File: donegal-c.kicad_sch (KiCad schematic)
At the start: 166 parts, among them J2 ISP, SW1 SW_SPST, SW10 SW_SPST, SW11 SW_SPST, SW12 SW_SPST, SW13 SW_SPST, SW14 SW_SPST, SW15 SW_SPST, SW16 SW_SPST, SW17 SW_SPST, SW18 SW_SPST, SW19 SW_SPST, SW2 SW_SPST, SW20 SW_SPST, SW21 SW_SPST, SW22 SW_SPST, SW23 SW_SPST, SW24 SW_SPST, SW25 SW_SPST, SW26 SW_SPST, SW27 SW_SPST, SW28 SW_SPST, SW29 SW_SPST, SW3 SW_SPST, SW30 SW_SPST, SW31 SW_SPST, SW32 SW_SPST, SW33 SW_SPST, SW34 SW_SPST, SW35 SW_SPST, SW36 SW_SPST, SW37 SW_SPST, SW38 SW_SPST, SW39 SW_SPST, SW4 SW_SPST, SW40 SW_SPST, SW41 SW_SPST, SW42 SW_SPST, SW43 SW_SPST, SW44 SW_SPST, SW45 SW_SPST, SW46 SW_SPST, SW47 SW_SPST, SW48 SW_SPST, SW49 SW_SPST, SW5 SW_SPST, SW50 SW_SPST, SW51 SW_SPST, SW52 SW_SPST, SW53 SW_SPST, SW54 SW_SPST, SW55 SW_SPST, SW56 SW_SPST, SW57 SW_SPST, SW58 SW_SPST, SW59 SW_SPST, SW6 SW_SPST, SW60 SW_SPST, SW61 SW_SPST, SW62 SW_SPST, SW63 SW_SPST, SW64 SW_SPST, SW65 SW_SPST, SW66 SW_SPST, SW67 SW_SPST, SW68 RESET, SW69 BOOT, SW7 SW_SPST, SW70 SW_SPST, SW71 SW_SPST, SW72 SW_SPST, SW8 SW_SPST, SW9 SW_SPST, U1 ATmega328-PU, Y1 16MHZ

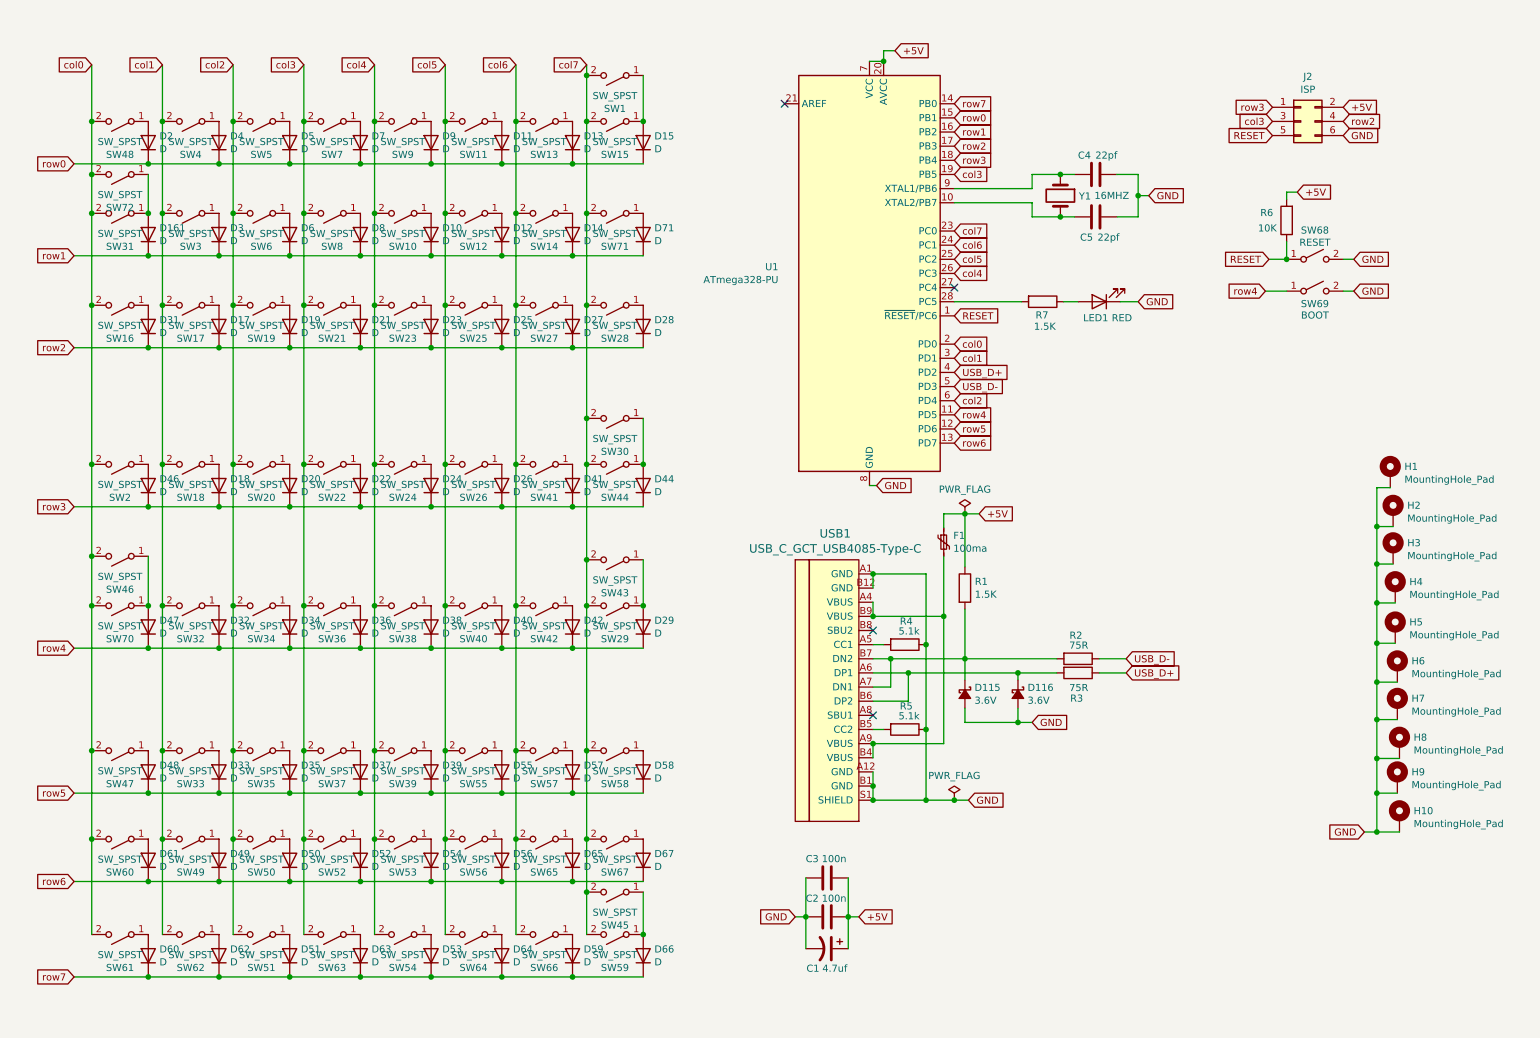
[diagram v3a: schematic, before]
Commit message: Update to v1.2
* Add Tsangan bottom row support
* Switch to MX_Alps_Hybrid MX_Only switch footprints
* Re-add the indicator LED to schematic
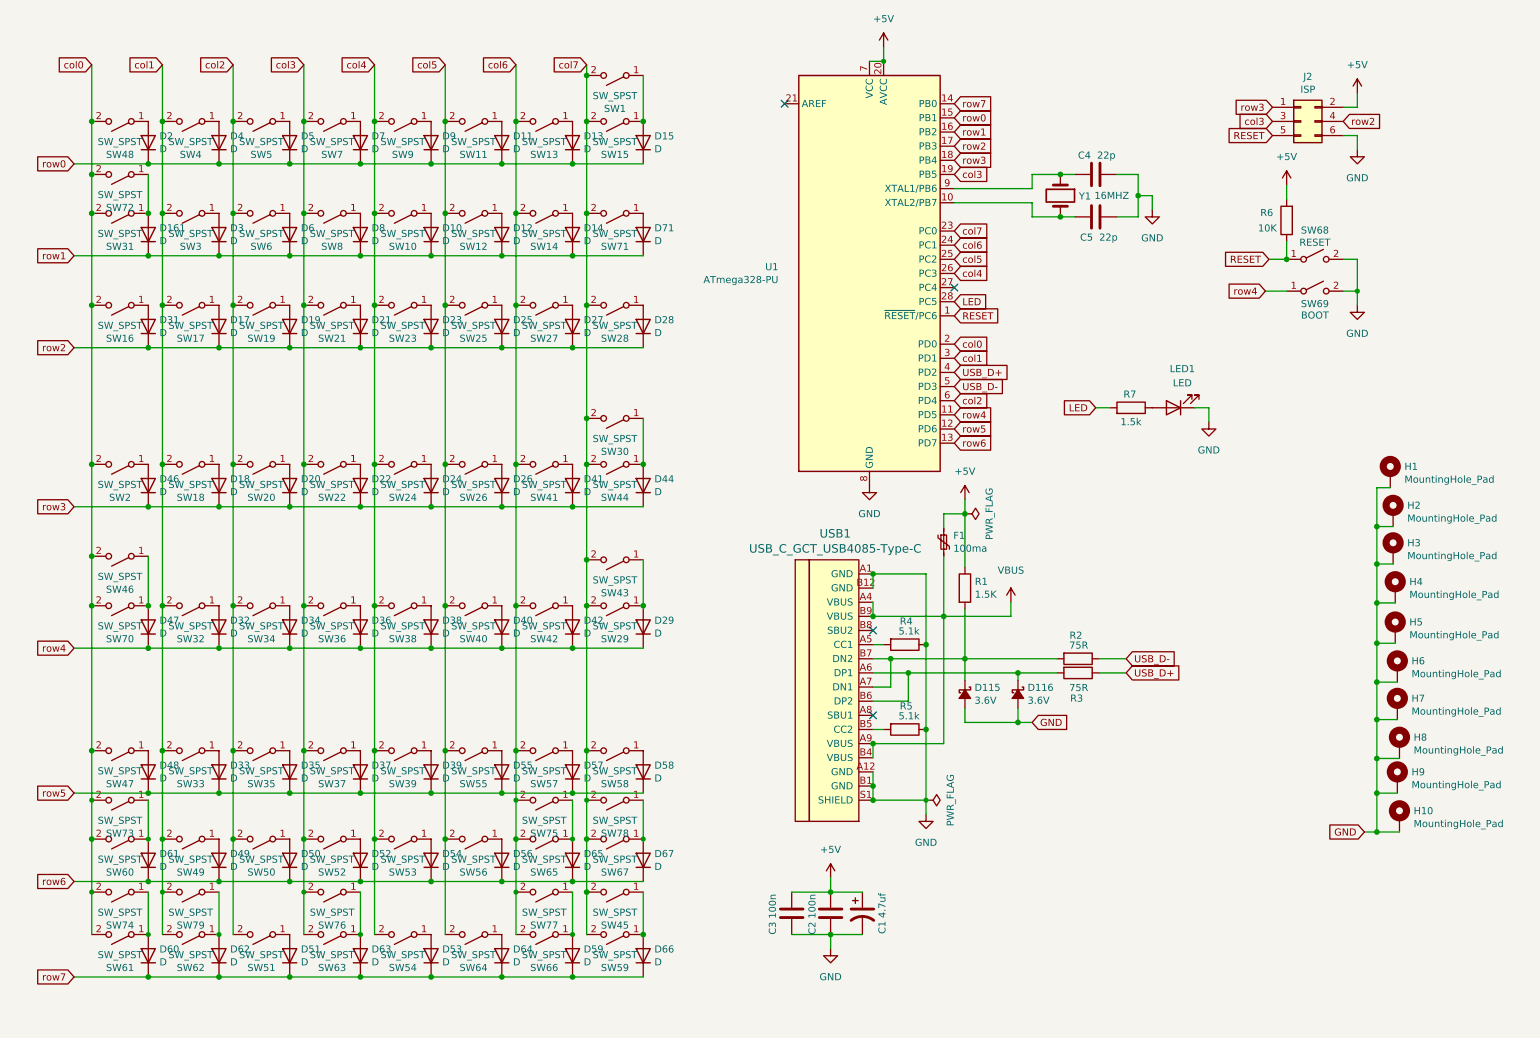
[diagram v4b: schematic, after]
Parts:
- added SW73, SW75, SW78, SW79: SW_SPST, MX_Only:MXOnly-1.5U-NoLED, symbol Switch:SW_SPST
- added SW74, SW77: SW_SPST, MX_Only:MXOnly-1U-NoLED, symbol Switch:SW_SPST
- added SW76: SW_SPST, MX_Only:MXOnly-7U-ReversedStabilizers-NoLED, symbol Switch:SW_SPST
- C4, C5: value 22pf -> 22p
- LED1: value RED -> LED
- R7: value 1.5K -> 1.5k
- SW1: footprint alpsmx:MX-2U-NoLED -> MX_Only:MXOnly-2U-NoLED
- SW10, SW11, SW12, SW13, SW14, SW15, SW17, SW18, SW19, SW2, SW20, SW21, SW22, SW23, SW24, SW25, SW26, SW27, SW28, SW29, SW3, SW32, SW33, SW34, SW35, SW36, SW37, SW38, SW39, SW4, SW40, SW41, SW42, SW47, SW48, SW49, SW5, SW50, SW51, SW52, SW53, SW54, SW55, SW56, SW57, SW58, SW6, SW7, SW71, SW8, SW9: footprint alpsmx:MX-1U-NoLED -> MX_Only:MXOnly-1U-NoLED
- SW16, SW43: footprint alpsmx:MX-1.5U-NoLED -> MX_Only:MXOnly-1.5U-NoLED
- SW30: footprint random:MX-ISO-ReversedStabilizersedit -> MX_Only:MXOnly-ISO-ROTATED-ReversedStabilizers-NoLED
- SW31: footprint tartan:SW_Cherry_MX1A_1.75u_PCBNOSCREEN -> MX_Only:MXOnly-1.75U-NoLED
- SW44, SW46: footprint alpsmx:MX-2.25U-NoLED -> MX_Only:MXOnly-2.25U-NoLED
- SW45: footprint alpsmx:MX-2.75U-NoLED -> MX_Only:MXOnly-2.75U-NoLED
- SW59: footprint alpsmx:MX-1.75U-NoLED -> MX_Only:MXOnly-1U-NoLED
- SW60, SW67, SW70: footprint alpsmx:MX-1.25U-NoLED -> MX_Only:MXOnly-1.25U-NoLED
- SW61, SW62, SW64, SW65, SW66: footprint alpsmx:MX-1.25U-NoLED -> MX_Only:MXOnly-1.5U-NoLED
- SW63: footprint alpsmx:MX-6.25U-ReversedStabilizers-NoLED -> MX_Only:MXOnly-6.25U-ReversedStabilizers-NoLED
- SW72: footprint tartan:SW_Cherry_MX1A_1.25u_PCBNOSCREEN -> MX_Only:MXOnly-1.25U-NoLED
- USB1: footprint tartan:USB_C_GCT_USB4085 -> 42keebs:USB_C_GCT_USB4085-offset-pads
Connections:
- net col0: now also SW73.2 (B), SW74.2 (B)
- net col1: now also SW79.2 (B)
- net col3: now also SW76.2 (B)
- net col6: now also SW75.2 (B), SW77.2 (B)
- net col7: now also SW78.2 (B)
- net at D61.2 (A), SW60.1 (A): now also SW73.1 (A)
- net at D65.2 (A), SW65.1 (A): now also SW75.1 (A)
- net at D67.2 (A), SW67.1 (A): now also SW78.1 (A)
- net at D59.2 (A), SW66.1 (A): now also SW77.1 (A)
- net at D60.2 (A), SW61.1 (A): now also SW74.1 (A)
- net at D62.2 (A), SW62.1 (A): now also SW79.1 (A)
- net at D63.2 (A), SW63.1 (A): now also SW76.1 (A)
- net LED: now reaches R7.2, U1.28 (PC5)
- net VBUS: now reaches F1.2, USB1.A4 (VBUS), USB1.A9 (VBUS), USB1.B4 (VBUS), USB1.B9 (VBUS)
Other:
- moved on the sheet: C1, C2, C3

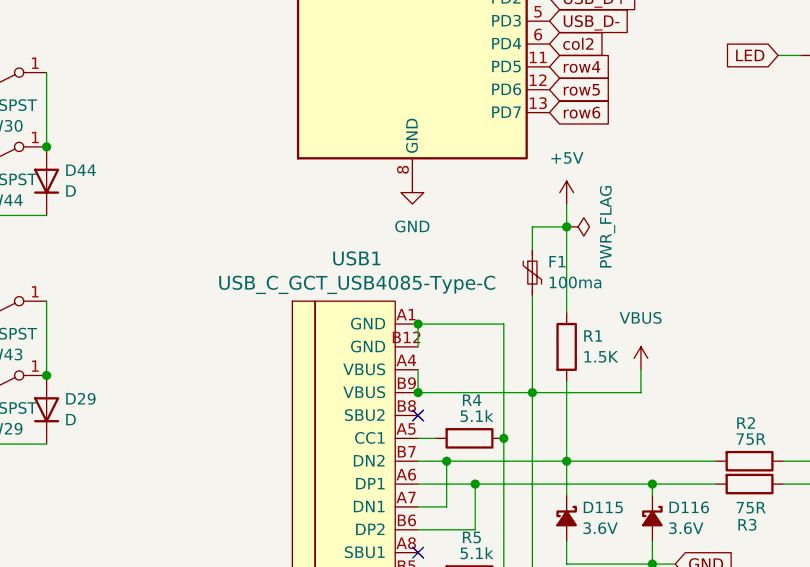
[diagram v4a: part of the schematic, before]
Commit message: Use USB-C socket symbol from the 42. Keebs library
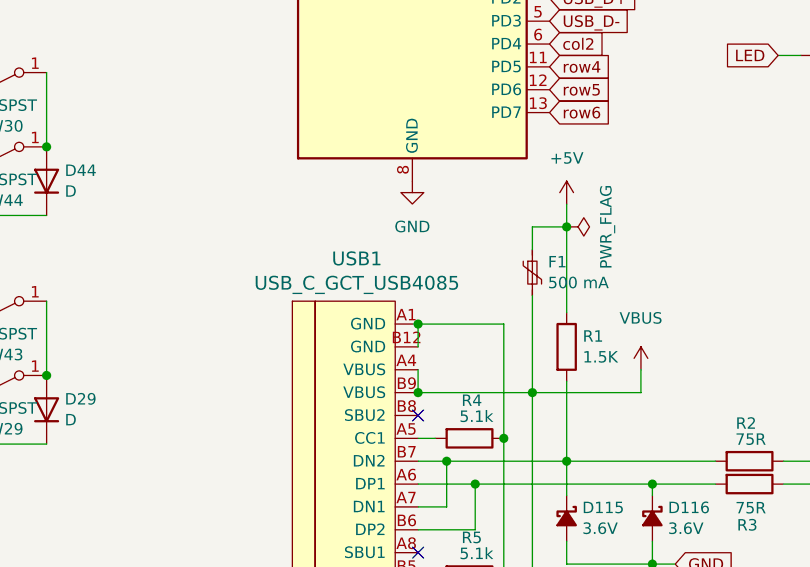
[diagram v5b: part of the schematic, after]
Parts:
- F1: value 100ma -> 500 mA
- USB1: value USB_C_GCT_USB4085-Type-C -> USB_C_GCT_USB4085; symbol donegal-c:USB_C_GCT_USB4085-Type-C -> 42keebs:USB_C_GCT_USB4085
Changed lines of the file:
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@@
       (effects (font (size 1.27 1.27)) (justify left))
     )
-    (property "Value" "100ma" (id 1) (at 179.5272 110.998 0)
+    (property "Value" "500 mA" (id 1) (at 179.5272 110.998 0)
       (effects (font (size 1.27 1.27)) (justify left))
     )
@@
     (pin "2")
   )
-  (symbol (lib_id "donegal-c:USB_C_GCT_USB4085-Type-C") (at 162.56 134.62 0) (unit 1)
+  (symbol (lib_id "42keebs:USB_C_GCT_USB4085") (at 162.56 134.62 0) (unit 1)
     (in_bom yes) (on_board yes)
     (property "Reference" "USB1" (id 0) (at 158.305 108.334 0)
       (effects (font (size 1.524 1.524)))
     )
-    (property "Value" "USB_C_GCT_USB4085-Type-C" (id 1) (at 158.3055 111.0411 0)
+    (property "Value" "USB_C_GCT_USB4085" (id 1) (at 158.3055 111.0411 0)
       (effects (font (size 1.524 1.524)))
     )
@@
     )
     (path "/00000000-0000-0000-0000-00005e210bf4"
-      (reference "F1") (unit 1) (value "100ma") (footprint "Capacitor_THT:C_Disc_D5.0mm_W2.5mm_P5.00mm")
+      (reference "F1") (unit 1) (value "500 mA") (footprint "Capacitor_THT:C_Disc_D5.0mm_W2.5mm_P5.00mm")
     )
     (path "/00000000-0000-0000-0000-00005df900c0"
@@
     )
     (path "/14cc5d03-4b82-4c1f-8c9a-4e49ee2a18b1"
-      (reference "USB1") (unit 1) (value "USB_C_GCT_USB4085-Type-C") (footprint "42keebs:USB_C_GCT_USB4085-offset-pads")
+      (reference "USB1") (unit 1) (value "USB_C_GCT_USB4085") (footprint "42keebs:USB_C_GCT_USB4085-offset-pads")
     )
     (path "/00000000-0000-0000-0000-00005e1e8d8f"

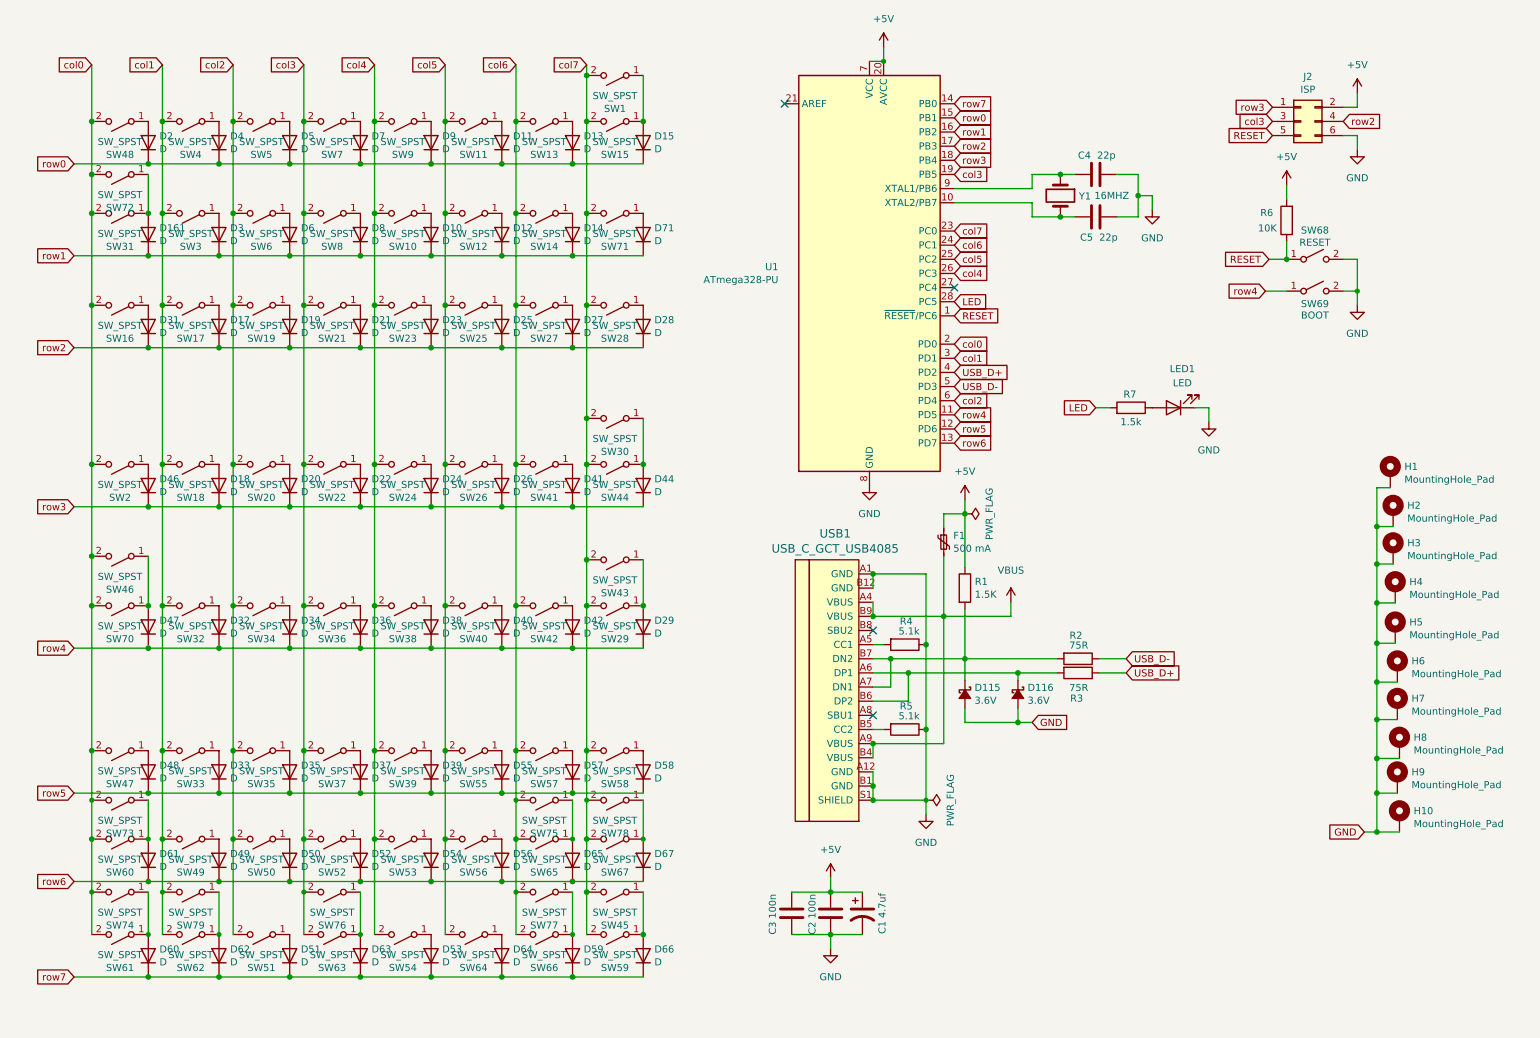
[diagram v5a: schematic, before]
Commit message: Fix incorrect bottom row sizes; add bottom row key labels
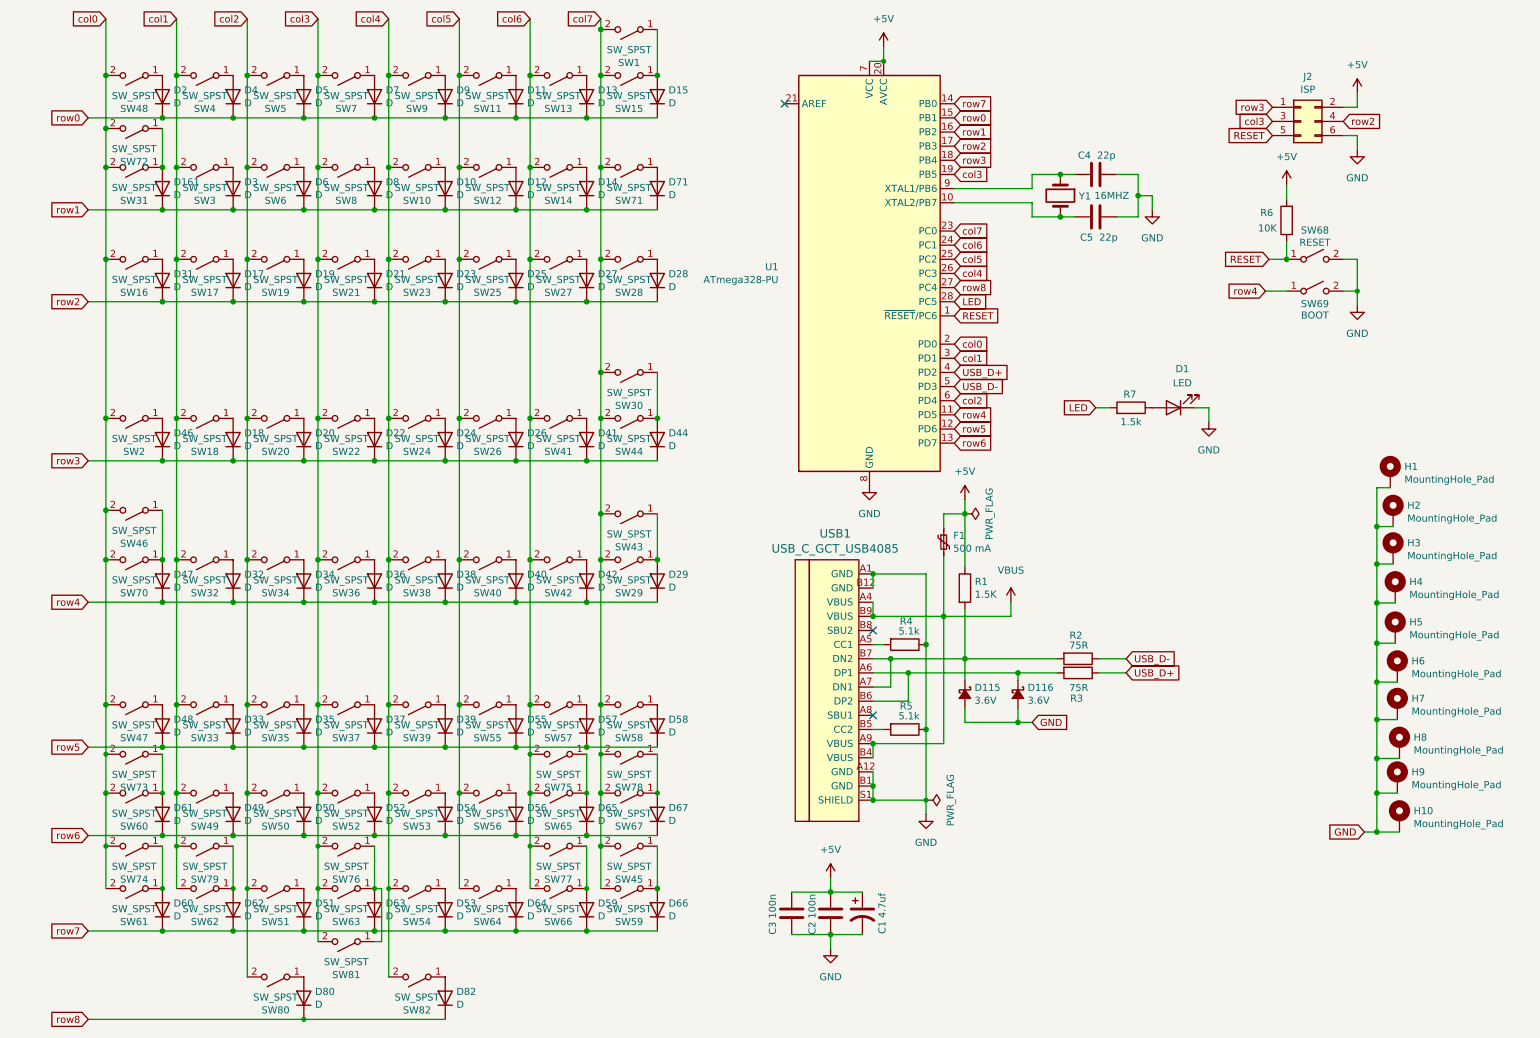
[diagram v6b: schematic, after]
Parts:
- added D80, D82: D, Diode_THT:D_DO-35_SOD27_P7.62mm_Horizontal, symbol Device:D
- added SW80: SW_SPST, MX_Only:MXOnly-2.75U-ReversedStabilizers-NoLED, symbol Switch:SW_SPST
- added SW81: SW_SPST, MX_Only:MXOnly-1.25U-NoLED, symbol Switch:SW_SPST
- added SW82: SW_SPST, MX_Only:MXOnly-2.25U-ReversedStabilizers-NoLED, symbol Switch:SW_SPST
- SW61, SW62, SW64, SW65, SW66: footprint MX_Only:MXOnly-1.5U-NoLED -> MX_Only:MXOnly-1.25U-NoLED
- renumbered LED1 to D1
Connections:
- net col2: now also SW80.2 (B)
- net col3: now also SW81.2 (B)
- net col4: now also SW82.2 (B)
- net at D63.2 (A), SW63.1 (A), SW76.1 (A): now also SW81.1 (A)
- net row8: now reaches U1.27 (PC4)
- net row8: now also D80.1 (K), D82.1 (K)
- new net: D80.2 (A), SW80.1 (A)
- new net: D82.2 (A), SW82.1 (A)
- no-connect marks 4 -> 3
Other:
- moved on the sheet: D10, D11, D12, D13, D14, D15, D161, D17, D18, D19, D2, D20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
